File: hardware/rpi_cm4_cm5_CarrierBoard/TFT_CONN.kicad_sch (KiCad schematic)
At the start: 20 parts, among them J8 62684-402100ALF, J9 5051101092

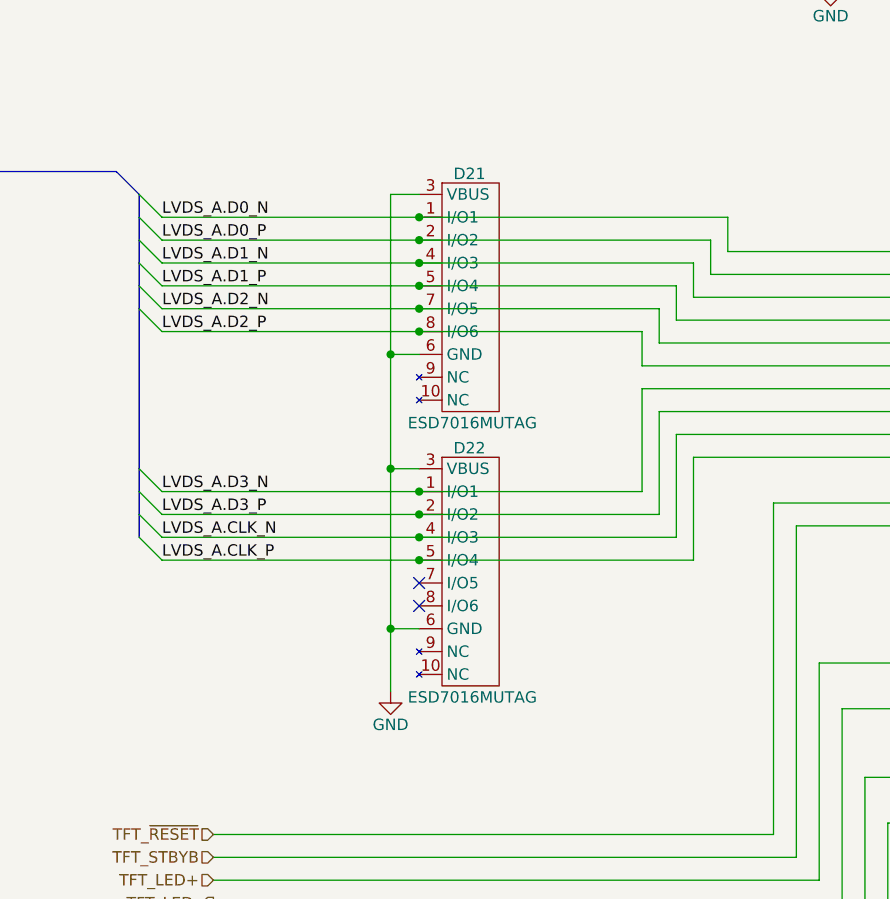
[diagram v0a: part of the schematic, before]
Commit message: Add power-up and power kill sequences Modify schematics to add net classes for DiffPairs
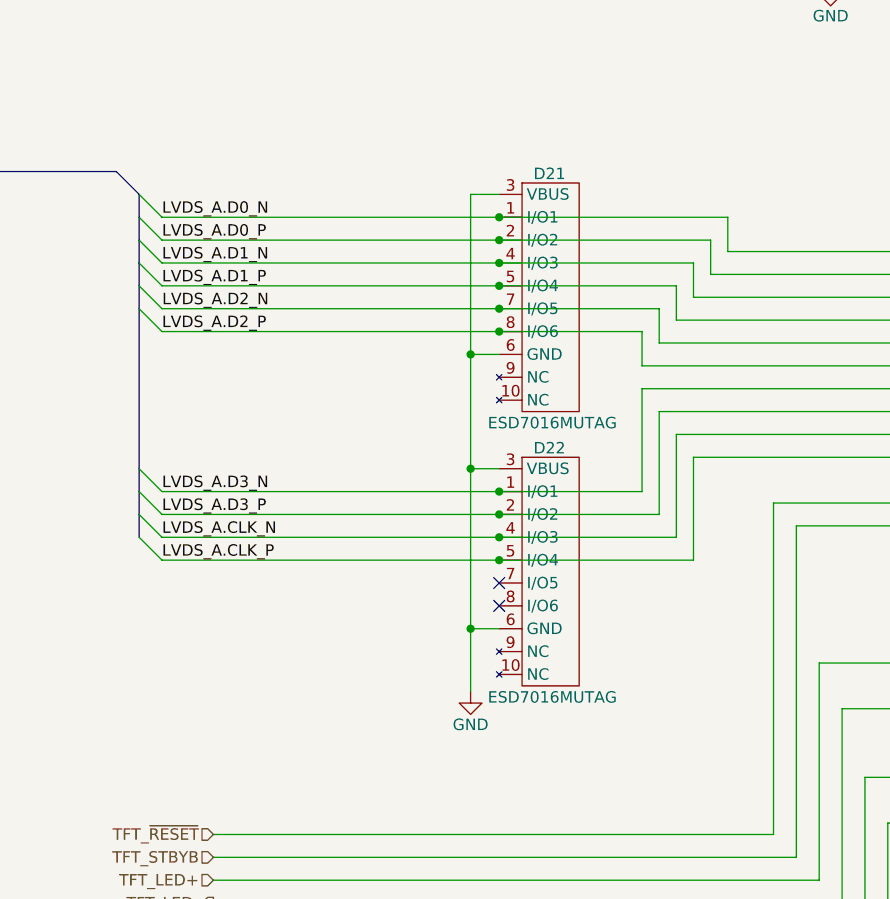
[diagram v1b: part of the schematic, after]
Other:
- moved on the sheet: D21, D22

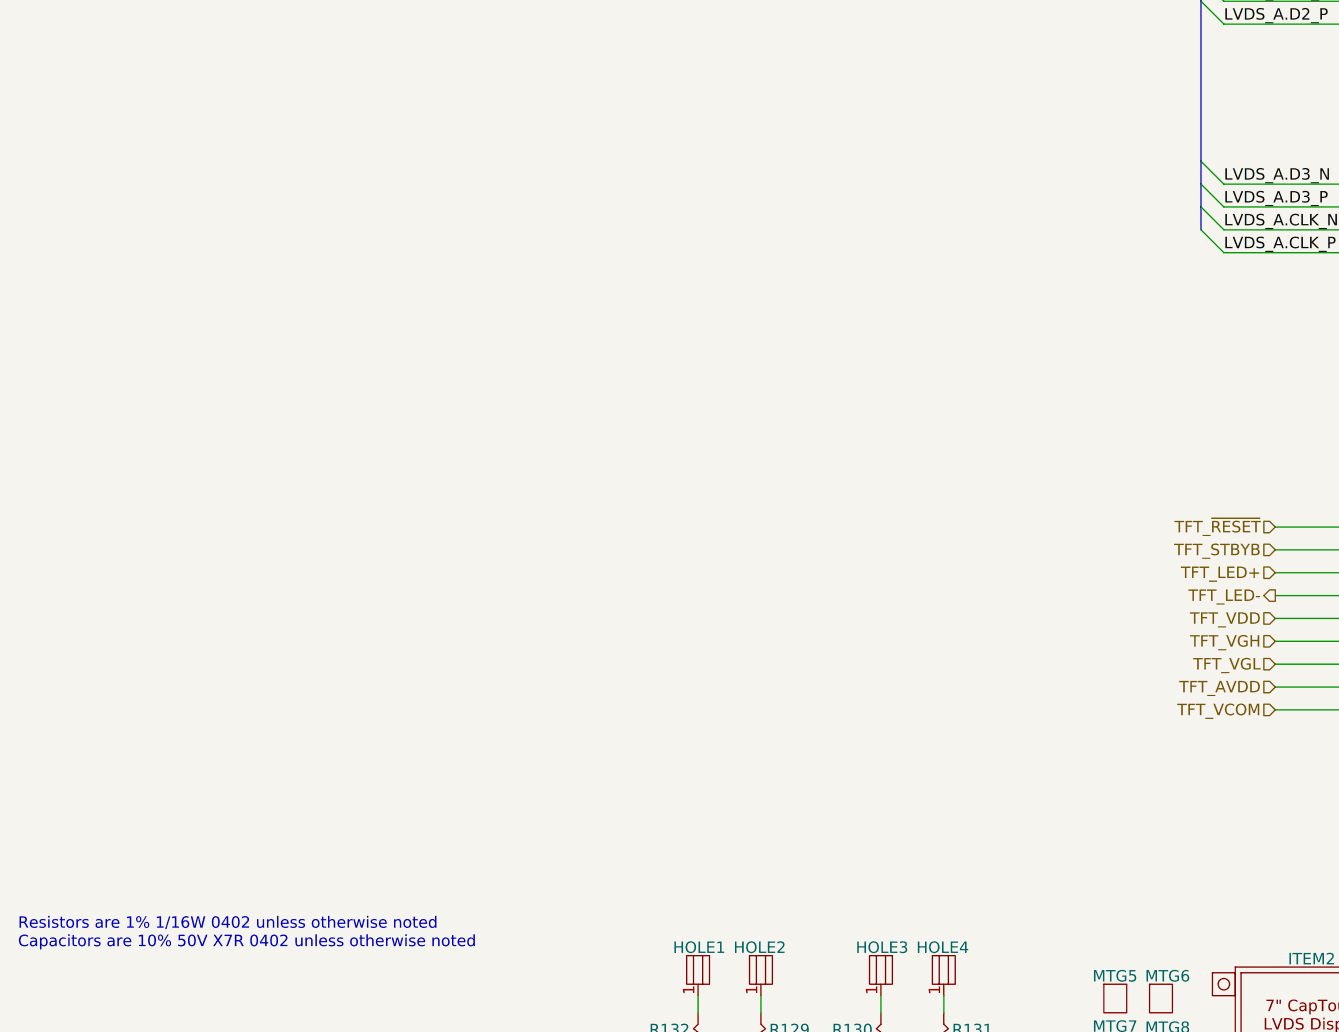
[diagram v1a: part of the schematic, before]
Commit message: Preliminary completion of RPI CMx schematics Cleaned up hierarchical root page
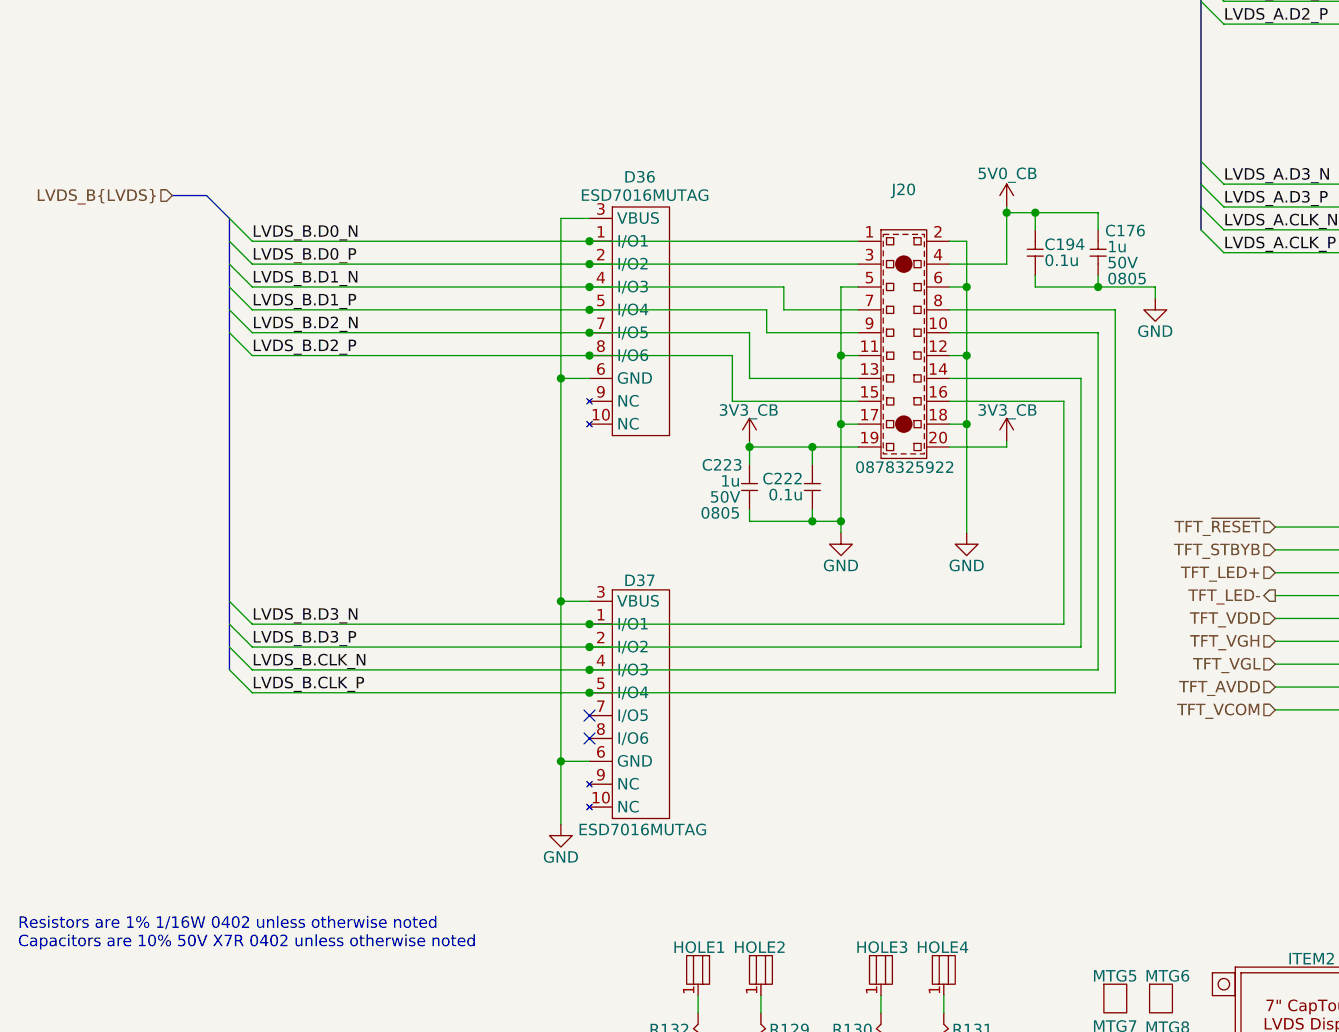
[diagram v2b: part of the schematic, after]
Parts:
- added C176, C223: 1u, footprint:CAP_NONPOL_0805, symbol KicadCompDb:Capacitors/CAP_CER_SMT_00002
- added C194, C222: 0.1u, footprint:CAP_NONPOL_0402, symbol KicadCompDb:Capacitors/CAP_CER_SMT_00001
- added D36, D37: ESD7016MUTAG, footprint:UDFN8, symbol KicadCompDb:ESD Diodes/ESD_DIODE_00001
- added J20: 0878325922, footprint:0878325922, symbol KicadCompDb:Connector/CONN_00020
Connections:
- net 5V0_CB: now also C176.2, C194.2, J20.4
- net GND: now also C176.1, C194.1, C222.1, C223.1, D36.3 (VBUS), D36.6 (GND), D37.3 (VBUS), D37.6 (GND), J20.11, J20.12, J20.17, J20.18, J20.2, J20.5, J20.6
- new net 3V3_CB: C222.2, C223.2, J20.19, J20.20
- new net LVDS_B.CLK_N: D37.4 (I/O3), J20.10
- new net LVDS_B.CLK_P: D37.5 (I/O4), J20.8
- new net LVDS_B.D0_N: D36.1 (I/O1), J20.1
- new net LVDS_B.D0_P: D36.2 (I/O2), J20.3
- new net LVDS_B.D1_N: D36.4 (I/O3), J20.7
- new net LVDS_B.D1_P: D36.5 (I/O4), J20.9
- new net LVDS_B.D2_N: D36.7 (I/O5), J20.13
- new net LVDS_B.D2_P: D36.8 (I/O6), J20.15
- new net LVDS_B.D3_N: D37.1 (I/O1), J20.16
- new net LVDS_B.D3_P: D37.2 (I/O2), J20.14
- no-connect marks 7 -> 9

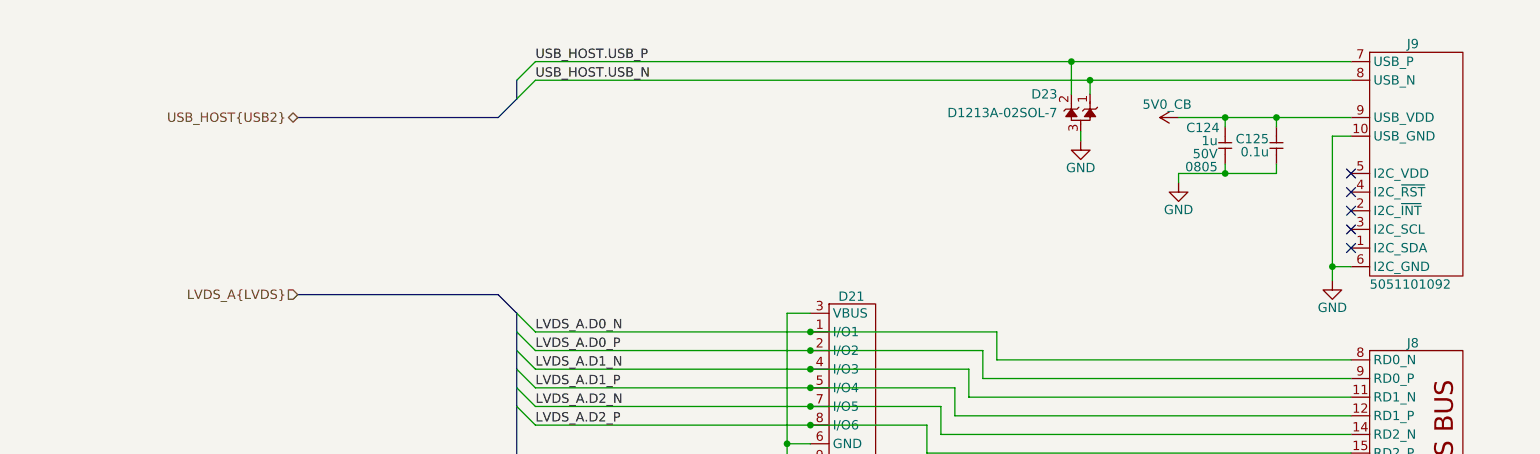
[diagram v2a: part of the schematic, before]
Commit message: Add preliminary BOM and preliminary .pdf schmematics Add BOM option for I2C control of ILI2132A for CapTouch HMI Add BOM options and DNP / 0R resistors for CM4 - CM5 build options
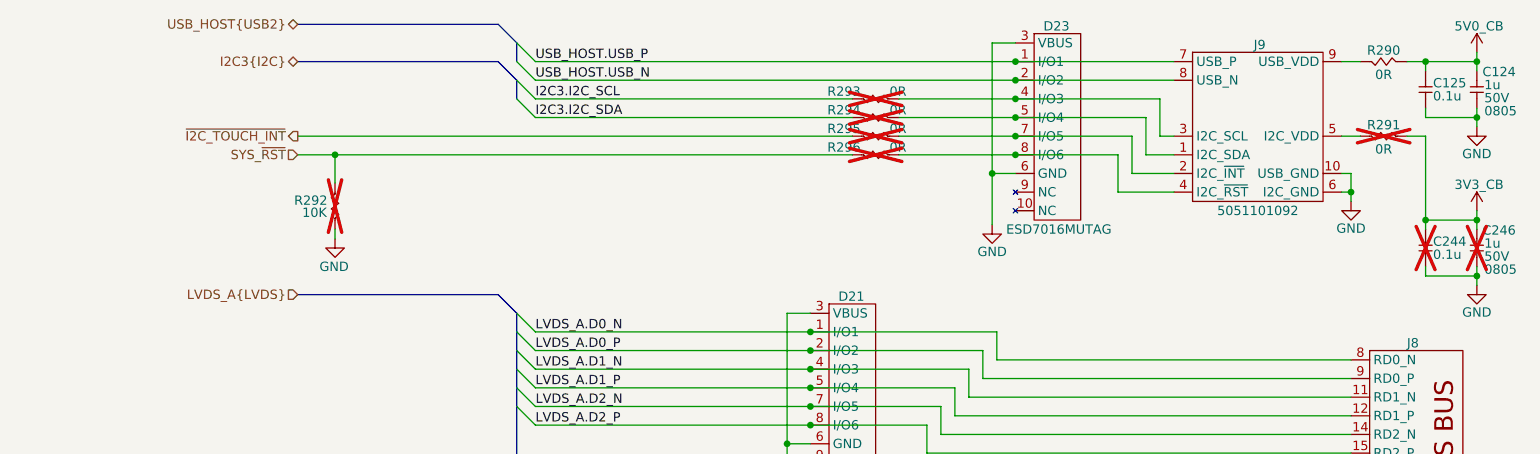
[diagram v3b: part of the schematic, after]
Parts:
- removed D23: D1213A-02SOL-7, footprint:SOT-23-3, symbol KicadCompDb:ESD Diodes/ESD_DIODE_00002
- removed J9: 5051101092, footprint:5051101092, symbol KicadCompDb:Connector/CONN_000017
- added C244: 0.1u, footprint:CAP_NONPOL_0402, symbol KicadCompDb:Capacitors/CAP_CER_SMT_00001
- added C246: 1u, footprint:CAP_NONPOL_0805, symbol KicadCompDb:Capacitors/CAP_CER_SMT_00002
- added D23: ESD7016MUTAG, footprint:UDFN8, symbol KicadCompDb:ESD Diodes/ESD_DIODE_00001
- added J9: 5051101092, footprint:5051101092, symbol KicadCompDb:Connector/CONN_00017
- added R290, R291, R293, R294, R295, R296: 0R, footprint:RES_0402, symbol KicadCompDb:Resistors/RES_SMT_00001
- added R292: 10K, footprint:RES_0402, symbol KicadCompDb:Resistors/RES_SMT_00013
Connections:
- net 3V3_CB: now also C244.2, C246.2, R291.1
- net 5V0_CB: now also R290.1
- net GND: now also C244.1, C246.1, D23.3 (VBUS), D23.6 (GND), J9.10 (USB_GND), J9.6 (I2C_GND), R292.1
- net USB_HOST.USB_N: now also D23.2 (I/O2), J9.8 (USB_N)
- net USB_HOST.USB_P: now also D23.1 (I/O1), J9.7 (USB_P)
- new net: J9.5 (I2C_VDD), R291.2
- new net: J9.9 (USB_VDD), R290.2
- new net: D23.8 (I/O6), J9.4 (I2C_~{RST}), R296.1
- new net: D23.5 (I/O4), J9.1 (I2C_SDA), R294.1
- new net: D23.7 (I/O5), J9.2 (I2C_~{INT}), R295.1
- new net: D23.4 (I/O3), J9.3 (I2C_SCL), R293.1
- new net I2C3.I2C_SCL: R293.2
- new net I2C3.I2C_SDA: R294.2
- new net SYS_~{RST}: R292.2, R296.2
- new net ~{I2C_TOUCH_INT}: R295.2
- no-connect marks 9 -> 4
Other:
- moved on the sheet: C124, C125

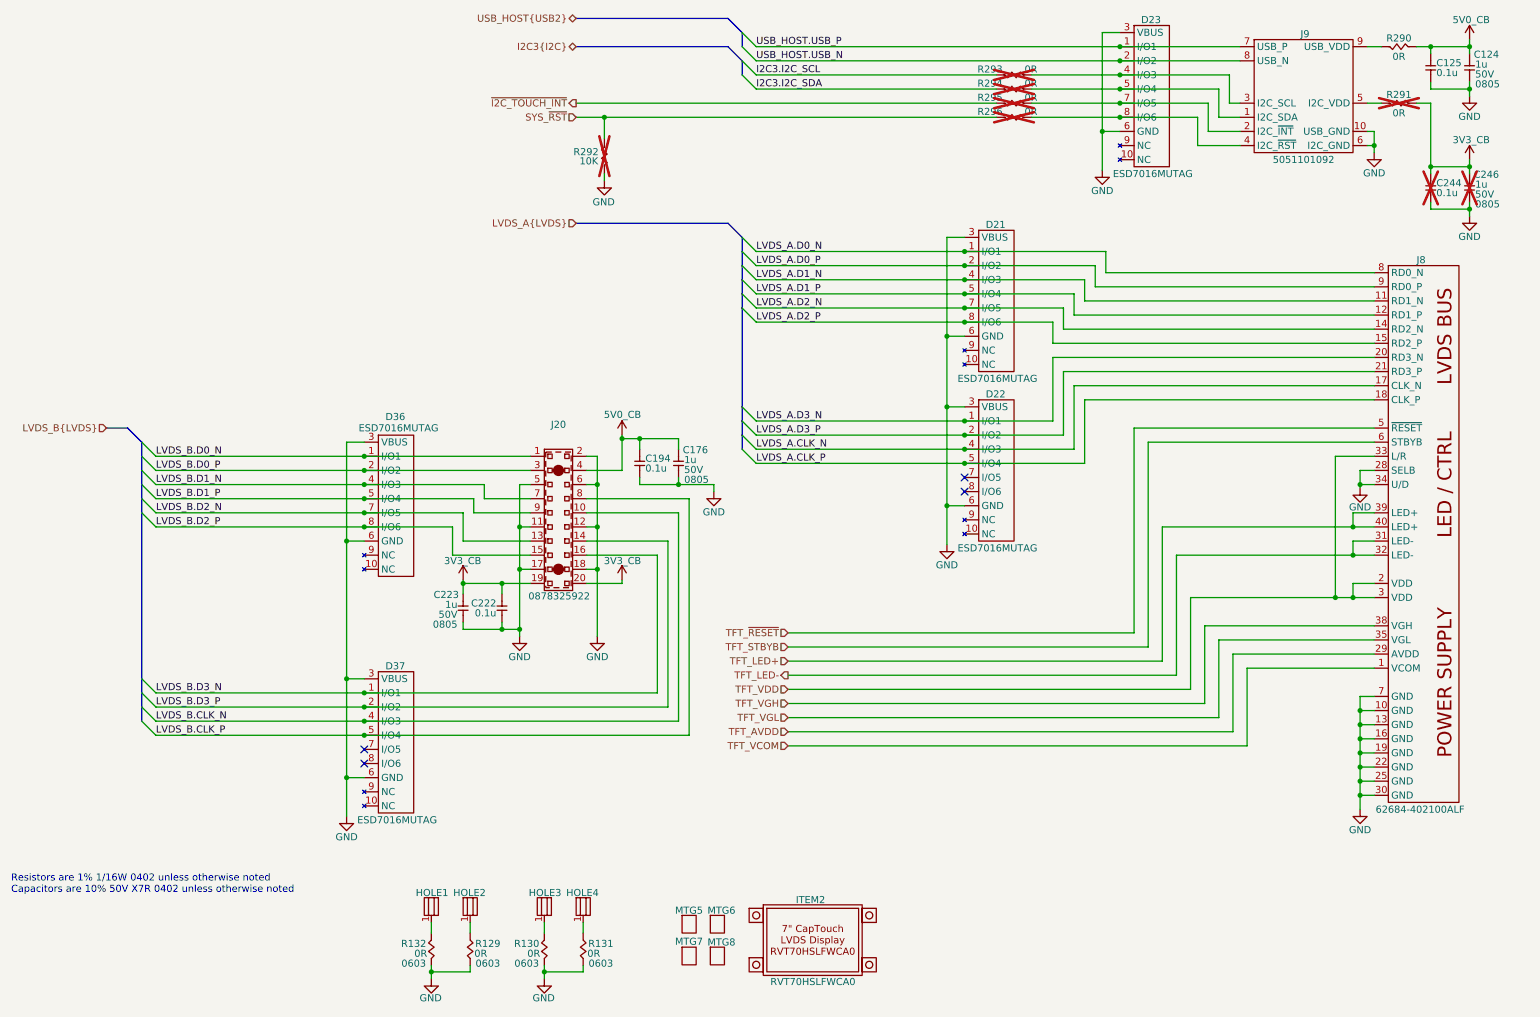
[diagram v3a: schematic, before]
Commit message: Added power input protection & filter Added dedicated QWIIC connector on RPI CMx I2C6 bus Adjusted power table and PinMux Updated schematics accordingly
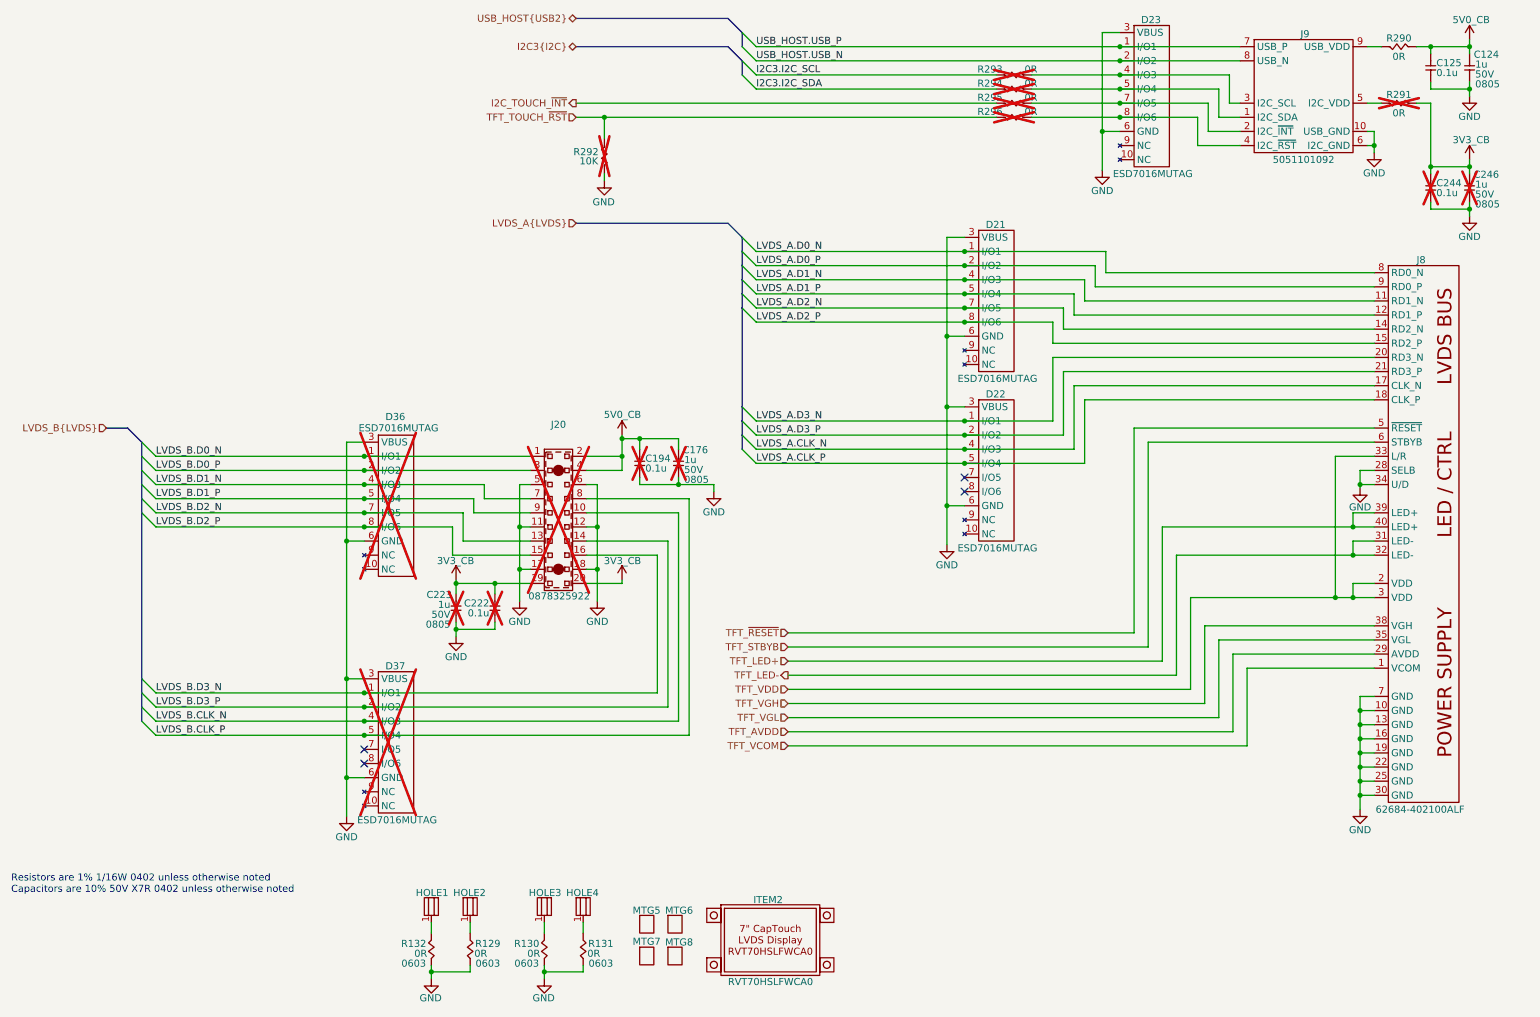
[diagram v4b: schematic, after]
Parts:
- C176, C194, C222, C223, D36, D37, J20: now not fitted
- ITEM2, MTG5, MTG6, MTG7, MTG8: now left out of the parts list
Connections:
- net 5V0_CB: now also J20.2
- net GND: no longer J20.2
- net SYS_~{RST} renamed TFT_TOUCH_~{RST}
- net ~{I2C_TOUCH_INT} renamed I2C_TOUCH_~{INT}
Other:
- moved on the sheet: ITEM2, MTG5, MTG6, MTG7, MTG8
